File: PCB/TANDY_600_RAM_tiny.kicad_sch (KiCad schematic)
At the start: 5 parts, among them J1 DIN 41612 2x22 male right-ang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, U1 628128_TSOP, U2 74HC08

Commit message: gnd on tiny, new dual sch, bus connector symbol & footprint
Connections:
- net A0: now also J1.b12; no longer J1.12B
- net A1: now also J1.a12; no longer J1.12A
- net A10: now also J1.b6; no longer J1.6B
- net A11: now also J1.a6; no longer J1.6A
- net A12: now also J1.a5; no longer J1.5A
- net A13: now also J1.b4; no longer J1.4B
- net A14: now also J1.a4; no longer J1.4A
- net A2: now also J1.b11; no longer J1.11B
- net A3: now also J1.a11; no longer J1.11A
- net A4: now also J1.a10; no longer J1.10A
- net A5: now also J1.b9; no longer J1.9B
- net A6: now also J1.a9; no longer J1.9A
- net A7: now also J1.b8; no longer J1.8B
- net A8: now also J1.b7; no longer J1.7B
- net A9: now also J1.a7; no longer J1.7A
- net CS2: now also J1.b21; no longer J1.21B
- net D0: now also J1.b17; no longer J1.17B
- net D1: now also J1.a17; no longer J1.17A
- net D2: now also J1.b16; no longer J1.16B
- net D3: now also J1.a16; no longer J1.16A
- net D4: now also J1.a15; no longer J1.15A
- net D5: now also J1.b14; no longer J1.14B
- net D6: now also J1.a14; no longer J1.14A
- net D7: now also J1.b13; no longer J1.13B
- net GND: now also J1.M1 (mount), J1.M2 (mount), J1.a13, J1.a18, J1.a19, J1.a22, J1.a3, J1.a8, J1.b10, J1.b22, J1.b5; no longer J1.10B, J1.13A, J1.18A, J1.19A, J1.22A, J1.22B, J1.3A, J1.5B, J1.8A, J1.S1 (mount), J1.S2 (mount)
- net VCC: now also J1.a2, J1.b2; no longer J1.2A, J1.2B
- net VMEM: now also J1.a1, J1.b1; no longer J1.1A, J1.1B
- net ~{CS1_A}: now also J1.b3; no longer J1.3B
- net ~{CS1_B}: now also J1.b20; no longer J1.20B
- net ~{CS1_C}: now also J1.a20; no longer J1.20A
- net ~{OE}: now also J1.b18; no longer J1.18B
- net ~{WE}: now also J1.b19; no longer J1.19B
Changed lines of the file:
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@@
   (title_block
     (title "96K RAM for TANDY 600")
-    (date "2022-09-27")
-    (rev "010")
+    (date "2022-10-04")
+    (rev "tiny_011")
     (company "Brian K. White - b.kenyon.w@gmail.com")
     (comment 1 "LICENSE: CC-BY-SA 4.0")
@@
     (pin "2")
   )
-  (symbol (lib_id "000_LOCAL:DIN 41612 2x22 male right-angle") (at 71.12 76.2 0) (unit 1)
+  (symbol (lib_id "000_LOCAL:DIN 41612 2x22 male right-angle") (at 72.39 77.47 0) (unit 1)
     (in_bom yes) (on_board yes)
-    (property "Reference" "J1" (id 0) (at 72.263 37.719 0))
-    (property "Value" "DIN 41612 2x22 male right-angle" (id 1) (at 74.168 40.64 0))
-    (property "Footprint" "000_LOCAL:DIN 41612 2x22 male right-angle" (id 2) (at 71.12 76.2 0)
+    (property "Reference" "J1" (id 0) (at 73.533 38.989 0))
+    (property "Value" "DIN 41612 2x22 male right-angle" (id 1) (at 75.438 41.91 0))
+    (property "Footprint" "000_LOCAL:DIN 41612 2x22 male right-angle" (id 2) (at 72.39 77.47 0)
       (effects (font (size 1.27 1.27)) hide)
     )
-    (property "Datasheet" "~" (id 3) (at 71.12 76.2 0)
+    (property "Datasheet" "~" (id 3) (at 72.39 77.47 0)
       (effects (font (size 1.27 1.27)) hide)
     )
-    (pin "10A")
-    (pin "10B")
-    (pin "11A")
-    (pin "11B")
-    (pin "12A")
-    (pin "12B")
-    (pin "13A")
-    (pin "13B")
-    (pin "14A")
-    (pin "14B")
-    (pin "15A")
-    (pin "15B")
-    (pin "16A")
-    (pin "16B")
-    (pin "17A")
-    (pin "17B")
-    (pin "18A")
-    (pin "18B")
-    (pin "19A")
-    (pin "19B")
-    (pin "1A")
-    (pin "1B")
-    (pin "20A")
-    (pin "20B")
-    (pin "21A")
-    (pin "21B")
-    (pin "22A")
-    (pin "22B")
-    (pin "2A")
-    (pin "2B")
-    (pin "3A")
-    (pin "3B")
-    (pin "4A")
-    (pin "4B")
-    (pin "5A")
-    (pin "5B")
-    (pin "6A")
-    (pin "6B")
-    (pin "7A")
-    (pin "7B")
-    (pin "8A")
-    (pin "8B")
-    (pin "9A")
-    (pin "9B")
-    (pin "S1")
-    (pin "S2")
+    (pin "M1")
+    (pin "M2")
+    (pin "a1")
+    (pin "a10")
+    (pin "a11")
+    (pin "a12")
+    (pin "a13")
+    (pin "a14")
+    (pin "a15")
+    (pin "a16")
+    (pin "a17")
+    (pin "a18")
+    (pin "a19")
+    (pin "a2")
+    (pin "a20")
+    (pin "a21")
+    (pin "a22")
+    (pin "a3")
+    (pin "a4")
+    (pin "a5")
+    (pin "a6")
+    (pin "a7")
+    (pin "a8")
+    (pin "a9")
+    (pin "b1")
+    (pin "b10")
+    (pin "b11")
+    (pin "b12")
+    (pin "b13")
+    (pin "b14")
+    (pin "b15")
+    (pin "b16")
+    (pin "b17")
+    (pin "b18")
+    (pin "b19")
+    (pin "b2")
+    (pin "b20")
+    (pin "b21")
+    (pin "b22")
+    (pin "b3")
+    (pin "b4")
+    (pin "b5")
+    (pin "b6")
+    (pin "b7")
+    (pin "b8")
+    (pin "b9")
   )
   (symbol (lib_id "000_LOCAL:VCC") (at 85.725 154.94 0) (unit 1)

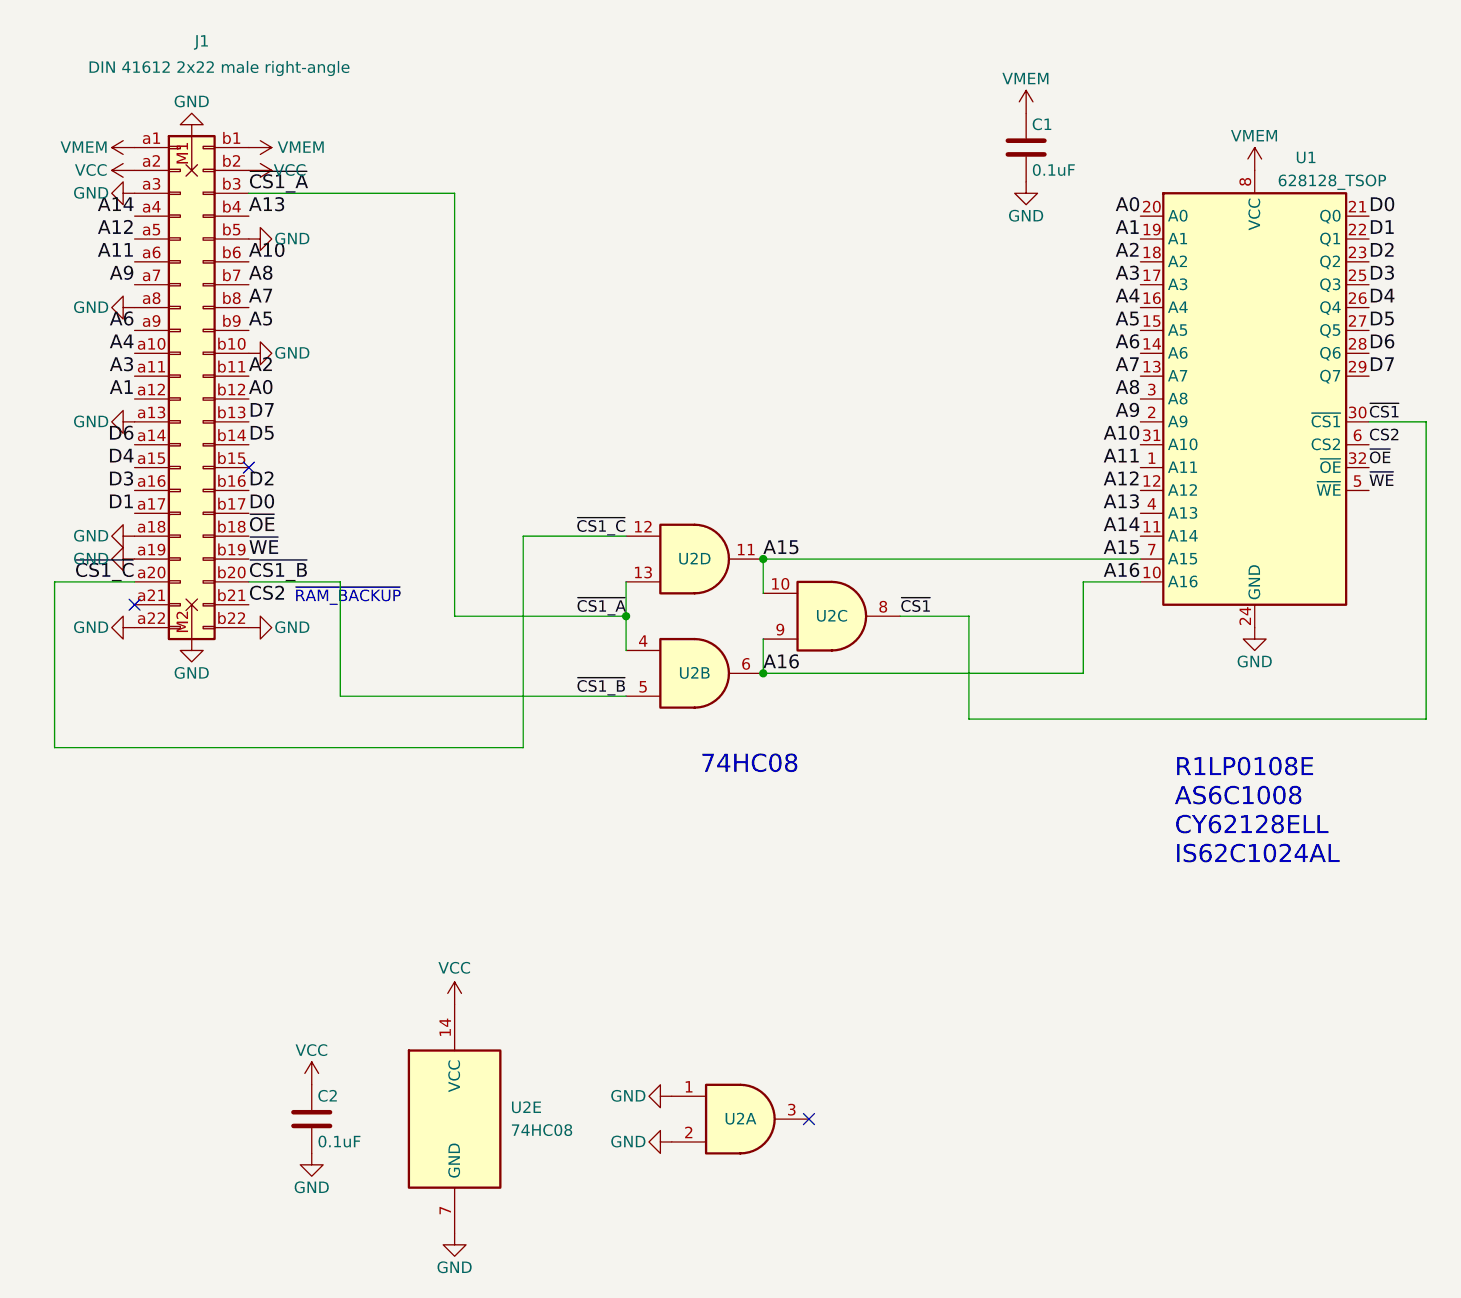
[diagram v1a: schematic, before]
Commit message: add full-size dual
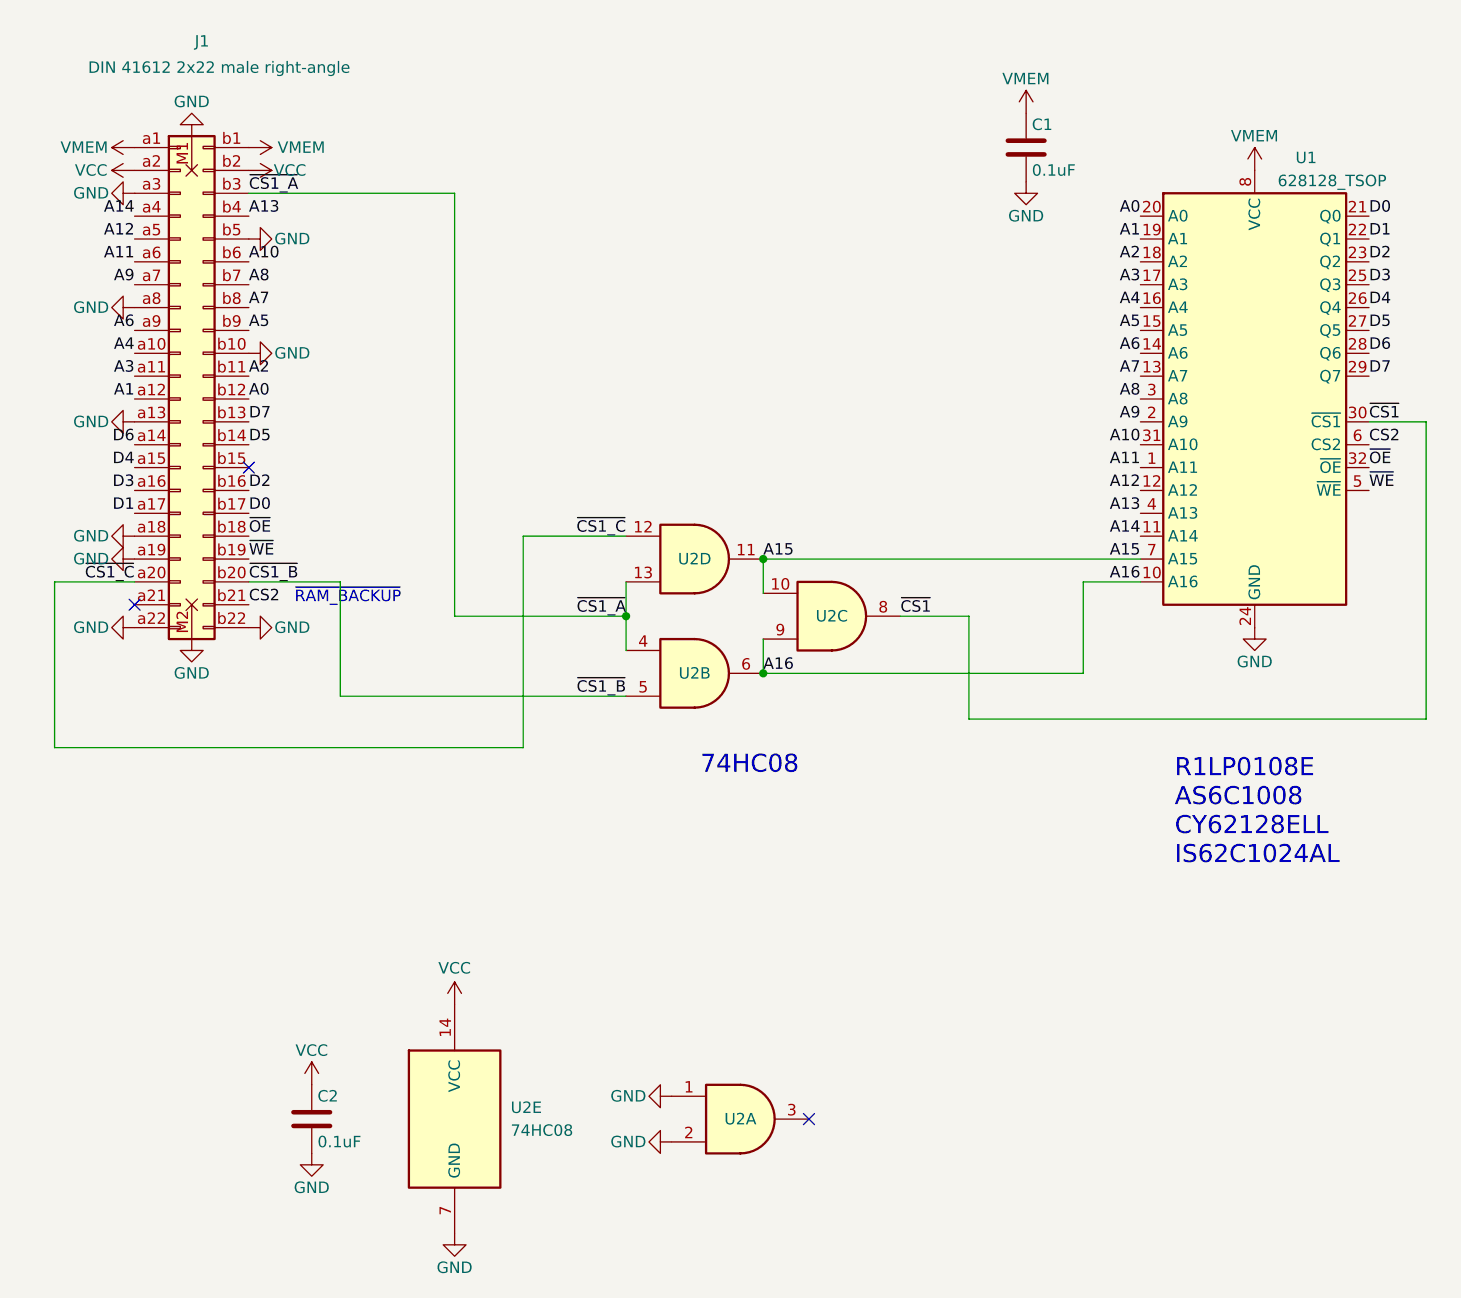
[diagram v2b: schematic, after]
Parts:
- J1: symbol 000_LOCAL:DIN 41612 2x22 male right-angle -> 000_LOCAL:DIN_41612_02x22

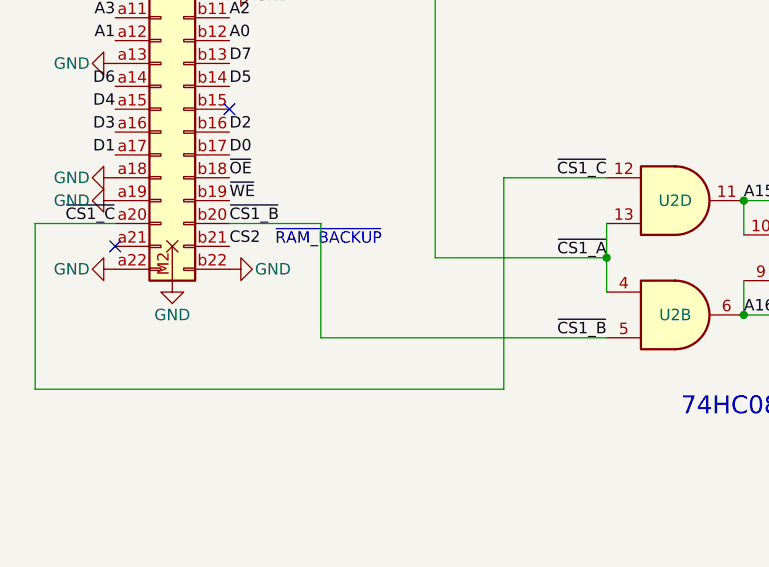
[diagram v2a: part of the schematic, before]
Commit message: footprints, ground paths
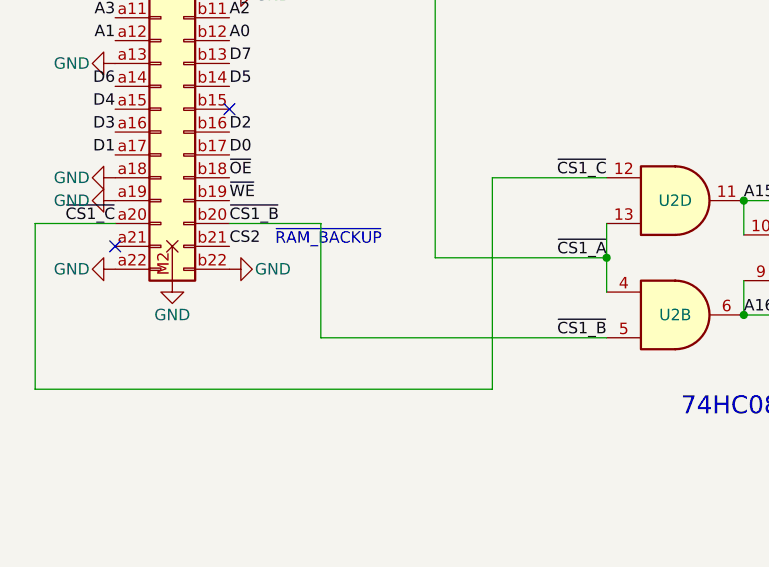
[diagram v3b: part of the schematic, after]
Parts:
- J1: footprint 000_LOCAL:DIN 41612 2x22 male right-angle -> 000_LOCAL:DIN-41612_02x22_male_horizontal
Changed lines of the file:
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@@
   (title_block
     (title "96K RAM for TANDY 600")
-    (date "2022-10-04")
-    (rev "tiny_011")
+    (date "2022-10-29")
+    (rev "tiny_012")
     (company "Brian K. White - b.kenyon.w@gmail.com")
-    (comment 1 "LICENSE: CC-BY-SA 4.0")
+    (comment 1 "CC-BY-SA")
     (comment 2 "Originally based on Model600Sram_v1.1 by Jayeson Lee-Steer")
     (comment 3 "Replaces TANDY Cat. No. 26-3910 \"OPRM\"")
@@
     (stroke (width 0) (type default) (color 0 0 0 0))
   )
-  (wire (pts (xy 109.22 93.98) (xy 109.22 117.475))
+  (wire (pts (xy 107.95 93.98) (xy 107.95 117.475))
     (stroke (width 0) (type default) (color 0 0 0 0))
   )
@@
     (stroke (width 0) (type default) (color 0 0 0 0))
   )
-  (wire (pts (xy 57.15 117.475) (xy 109.22 117.475))
+  (wire (pts (xy 57.15 117.475) (xy 107.95 117.475))
     (stroke (width 0) (type default) (color 0 0 0 0))
   )
@@
     (stroke (width 0) (type default) (color 0 0 0 0))
   )
-  (wire (pts (xy 109.22 93.98) (xy 120.65 93.98))
+  (wire (pts (xy 107.95 93.98) (xy 120.65 93.98))
     (stroke (width 0) (type default) (color 0 0 0 0))
   )
@@
     (property "Reference" "J1" (id 0) (at 73.533 38.989 0))
     (property "Value" "DIN 41612 2x22 male right-angle" (id 1) (at 75.438 41.91 0))
-    (property "Footprint" "000_LOCAL:DIN 41612 2x22 male right-angle" (id 2) (at 71.12 76.2 0)
+    (property "Footprint" "000_LOCAL:DIN-41612_02x22_male_horizontal" (id 2) (at 71.12 76.2 0)
       (effects (font (size 1.27 1.27)) hide)
     )
@@
     )
     (path "/00000000-0000-0000-0000-000061163f2f"
-      (reference "J1") (unit 1) (value "DIN 41612 2x22 male right-angle") (footprint "000_LOCAL:DIN 41612 2x22 male right-angle")
+      (reference "J1") (unit 1) (value "DIN 41612 2x22 male right-angle") (footprint "000_LOCAL:DIN-41612_02x22_male_horizontal")
     )
     (path "/00000000-0000-0000-0000-0000613c8a04"

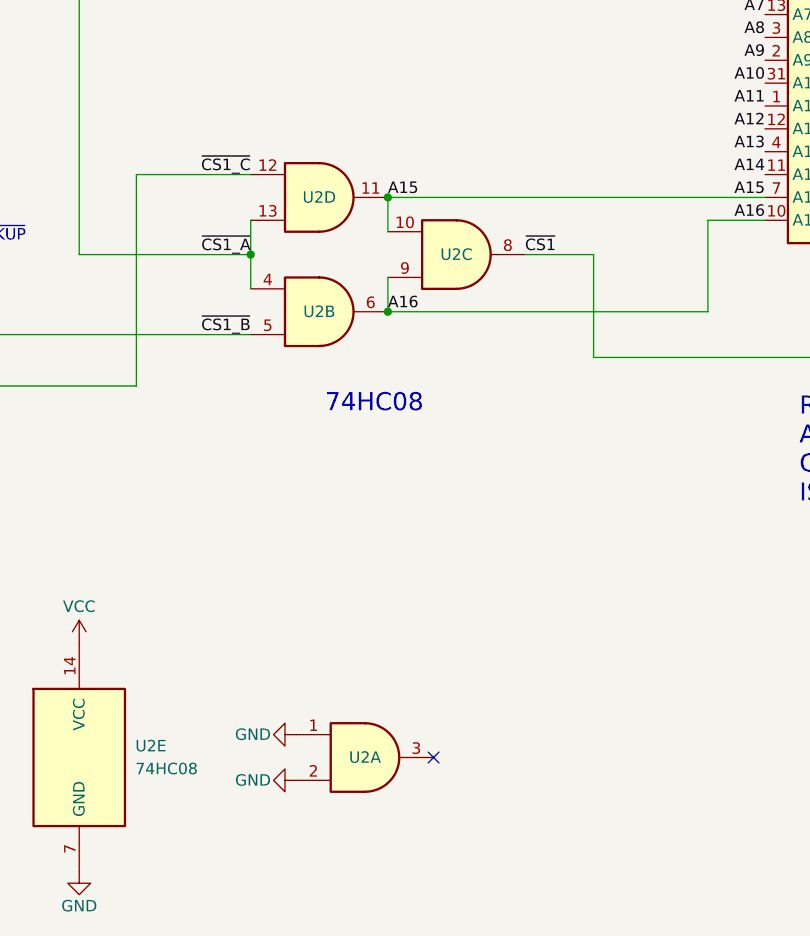
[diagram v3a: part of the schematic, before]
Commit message: dual version add /CE pullup for battery life
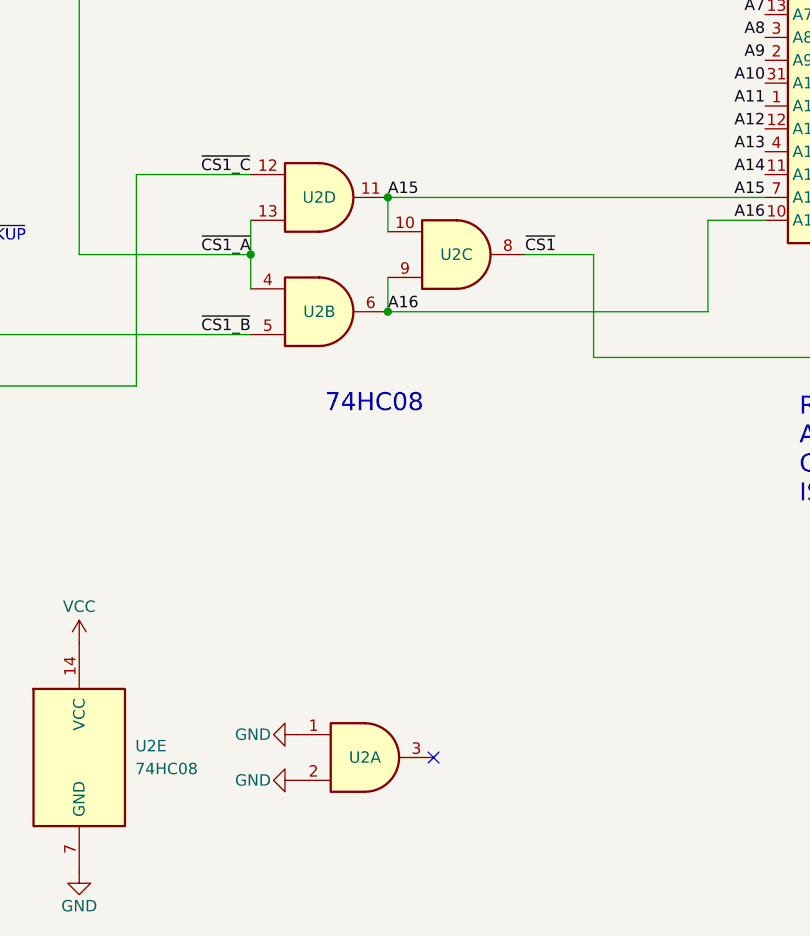
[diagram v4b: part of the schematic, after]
